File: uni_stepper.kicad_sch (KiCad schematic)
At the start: 2 parts, among them M201 unipolair motor, U201 ULN2003

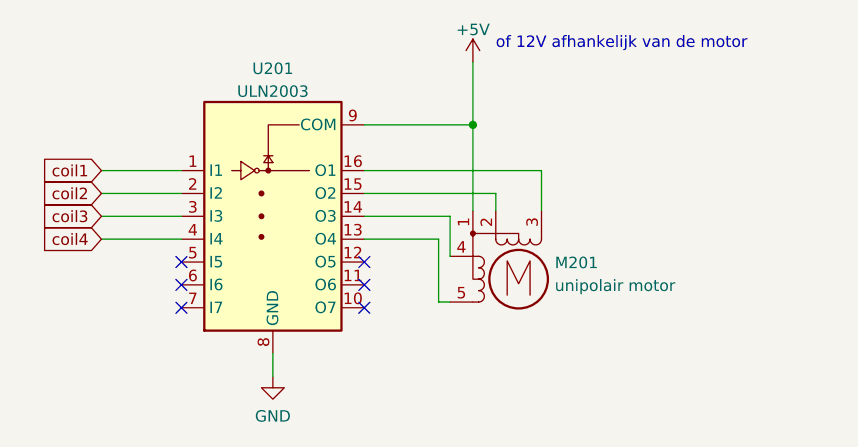
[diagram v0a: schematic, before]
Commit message: added hierarchial labels to some schematics
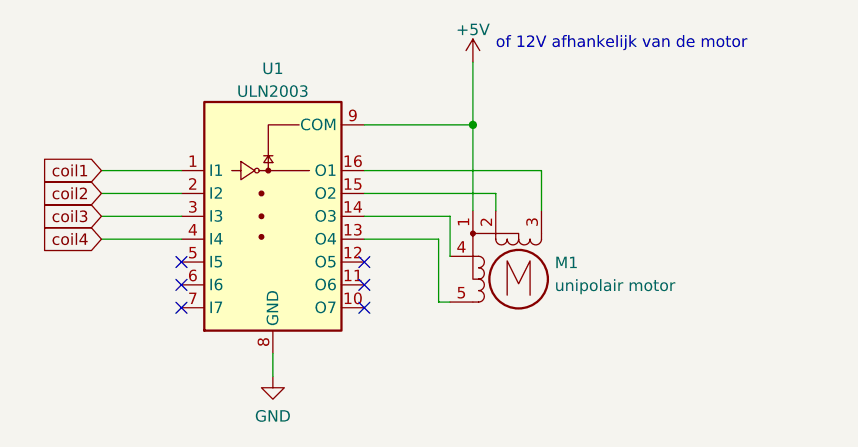
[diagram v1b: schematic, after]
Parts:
- renumbered M201 to M1, U201 to U1
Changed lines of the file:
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@@
-(kicad_sch (version 20211123) (generator eeschema)
+(kicad_sch (version 20230121) (generator eeschema)
   (paper "A4")
   (junction (at 127.635 73.66) (diameter 0) (color 0 0 0 0)
@@
   (no_connect (at 115.57 93.98))
   (wire (pts (xy 86.36 81.28) (xy 95.25 81.28))
-    (stroke (width 0) (type default) (color 0 0 0 0))
+    (stroke (width 0) (type default))
   )
   (wire (pts (xy 127.635 66.675) (xy 127.635 73.66))
-    (stroke (width 0) (type default) (color 0 0 0 0))
+    (stroke (width 0) (type default))
   )
   (wire (pts (xy 86.36 86.36) (xy 95.25 86.36))
-    (stroke (width 0) (type default) (color 0 0 0 0))
+    (stroke (width 0) (type default))
   )
   (wire (pts (xy 115.57 78.74) (xy 135.255 78.74))
-    (stroke (width 0) (type default) (color 0 0 0 0))
+    (stroke (width 0) (type default))
   )
   (wire (pts (xy 86.36 78.74) (xy 95.25 78.74))
-    (stroke (width 0) (type default) (color 0 0 0 0))
+    (stroke (width 0) (type default))
   )
   (wire (pts (xy 123.825 86.36) (xy 115.57 86.36))
-    (stroke (width 0) (type default) (color 0 0 0 0))
+    (stroke (width 0) (type default))
   )
   (wire (pts (xy 125.095 93.345) (xy 123.825 93.345))
-    (stroke (width 0) (type default) (color 0 0 0 0))
+    (stroke (width 0) (type default))
   )
   (wire (pts (xy 135.255 78.74) (xy 135.255 83.185))
-    (stroke (width 0) (type default) (color 0 0 0 0))
+    (stroke (width 0) (type default))
   )
   (wire (pts (xy 125.095 83.82) (xy 115.57 83.82))
-    (stroke (width 0) (type default) (color 0 0 0 0))
+    (stroke (width 0) (type default))
   )
   (wire (pts (xy 127.635 73.66) (xy 127.635 83.185))
-    (stroke (width 0) (type default) (color 0 0 0 0))
+    (stroke (width 0) (type default))
   )
   (wire (pts (xy 130.175 83.185) (xy 130.175 81.28))
-    (stroke (width 0) (type default) (color 0 0 0 0))
+    (stroke (width 0) (type default))
   )
   (wire (pts (xy 86.36 83.82) (xy 95.25 83.82))
-    (stroke (width 0) (type default) (color 0 0 0 0))
+    (stroke (width 0) (type default))
   )
   (wire (pts (xy 115.57 73.66) (xy 127.635 73.66))
-    (stroke (width 0) (type default) (color 0 0 0 0))
+    (stroke (width 0) (type default))
   )
   (wire (pts (xy 105.41 99.06) (xy 105.41 101.6))
-    (stroke (width 0) (type default) (color 0 0 0 0))
+    (stroke (width 0) (type default))
   )
   (wire (pts (xy 123.825 93.345) (xy 123.825 86.36))
-    (stroke (width 0) (type default) (color 0 0 0 0))
+    (stroke (width 0) (type default))
   )
   (wire (pts (xy 130.175 81.28) (xy 115.57 81.28))
-    (stroke (width 0) (type default) (color 0 0 0 0))
+    (stroke (width 0) (type default))
   )
   (wire (pts (xy 125.095 83.82) (xy 125.095 88.265))
-    (stroke (width 0) (type default) (color 0 0 0 0))
+    (stroke (width 0) (type default))
   )
   (text "of 12V afhankelijk van de motor\n" (at 130.175 65.405 0)
@@
   (global_label "coil4" (shape input) (at 86.36 86.36 180) (fields_autoplaced)
     (effects (font (size 1.27 1.27)) (justify right))
-    (property "Intersheet References" "${INTERSHEET_REFS}" (id 0) (at 79.2298 86.2806 0)
+    (property "Intersheetrefs" "${INTERSHEET_REFS}" (at 79.2298 86.2806 0)
       (effects (font (size 1.27 1.27)) (justify right) hide)
     )
@@
   (global_label "coil3" (shape input) (at 86.36 83.82 180) (fields_autoplaced)
     (effects (font (size 1.27 1.27)) (justify right))
-    (property "Intersheet References" "${INTERSHEET_REFS}" (id 0) (at 79.2298 83.7406 0)
+    (property "Intersheetrefs" "${INTERSHEET_REFS}" (at 79.2298 83.7406 0)
       (effects (font (size 1.27 1.27)) (justify right) hide)
     )
@@
   (global_label "coil1" (shape input) (at 86.36 78.74 180) (fields_autoplaced)
     (effects (font (size 1.27 1.27)) (justify right))
-    (property "Intersheet References" "${INTERSHEET_REFS}" (id 0) (at 79.2298 78.6606 0)
+    (property "Intersheetrefs" "${INTERSHEET_REFS}" (at 79.2298 78.6606 0)
       (effects (font (size 1.27 1.27)) (justify right) hide)
     )
@@
   (global_label "coil2" (shape input) (at 86.36 81.28 180) (fields_autoplaced)
     (effects (font (size 1.27 1.27)) (justify right))
-    (property "Intersheet References" "${INTERSHEET_REFS}" (id 0) (at 79.2298 81.2006 0)
+    (property "Intersheetrefs" "${INTERSHEET_REFS}" (at 79.2298 81.2006 0)
       (effects (font (size 1.27 1.27)) (justify right) hide)
     )
   )
   (symbol (lib_id "power:GND") (at 105.41 101.6 0) (unit 1)
-    (in_bom yes) (on_board yes) (fields_autoplaced)
-    (property "Reference" "#PWR0201" (id 0) (at 105.41 107.95 0)
-      (effects (font (size 1.27 1.27)) hide)
-    )
-    (property "Value" "GND" (id 1) (at 105.41 106.0434 0))
-    (property "Footprint" "" (id 2) (at 105.41 101.6 0)
-      (effects (font (size 1.27 1.27)) hide)
-    )
-    (property "Datasheet" "" (id 3) (at 105.41 101.6 0)
-      (effects (font (size 1.27 1.27)) hide)
-    )
-    (pin "1")
+    (in_bom yes) (on_board yes) (dnp no) (fields_autoplaced)
+    (property "Reference" "#PWR02" (at 105.41 107.95 0)
+      (effects (font (size 1.27 1.27)) hide)
+    )
+    (property "Value" "GND" (at 105.41 106.0434 0)
+      (effects (font (size 1.27 1.27)))
+    )
+    (property "Footprint" "" (at 105.41 101.6 0)
+      (effects (font (size 1.27 1.27)) hide)
+    )
+    (property "Datasheet" "" (at 105.41 101.6 0)
+      (effects (font (size 1.27 1.27)) hide)
+    )
+    (pin "1")
+    (instances
+      (project "general_schematics"
+        (path "/e777d9ec-d073-4229-a9e6-2cf85636e407/9476ca91-c6eb-46e7-bd6a-31c98618510b"
+          (reference "#PWR02") (unit 1)
+        )
+      )
+    )
   )
   (symbol (lib_id "Transistor_Array:ULN2003") (at 105.41 83.82 0) (unit 1)
-    (in_bom yes) (on_board yes) (fields_autoplaced)
-    (property "Reference" "U201" (id 0) (at 105.41 67.4202 0))
-    (property "Value" "ULN2003" (id 1) (at 105.41 69.9571 0))
-    (property "Footprint" "" (id 2) (at 106.68 97.79 0)
+    (in_bom yes) (on_board yes) (dnp no) (fields_autoplaced)
+    (property "Reference" "U1" (at 105.41 67.4202 0)
+      (effects (font (size 1.27 1.27)))
+    )
+    (property "Value" "ULN2003" (at 105.41 69.9571 0)
+      (effects (font (size 1.27 1.27)))
+    )
+    (property "Footprint" "" (at 106.68 97.79 0)
       (effects (font (size 1.27 1.27)) (justify left) hide)
     )
-    (property "Datasheet" "http://www.ti.com/lit/ds/symlink/uln2003a.pdf" (id 3) (at 107.95 88.9 0)
+    (property "Datasheet" "http://www.ti.com/lit/ds/symlink/uln2003a.pdf" (at 107.95 88.9 0)
       (effects (font (size 1.27 1.27)) hide)
     )
@@
     (pin "8")
     (pin "9")
+    (instances
+      (project "general_schematics"
+        (path "/e777d9ec-d073-4229-a9e6-2cf85636e407/9476ca91-c6eb-46e7-bd6a-31c98618510b"
+          (reference "U1") (unit 1)
+        )
+      )
+    )
   )
   (symbol (lib_id "Motor:Stepper_Motor_unipolar_5pin") (at 132.715 90.805 0) (unit 1)
-    (in_bom yes) (on_board yes) (fields_autoplaced)
-    (property "Reference" "M201" (id 0) (at 136.7282 88.9924 0)
+    (in_bom yes) (on_board yes) (dnp no) (fields_autoplaced)
+    (property "Reference" "M1" (at 136.7282 88.9924 0)
       (effects (font (size 1.27 1.27)) (justify left))
     )
-    (property "Value" "unipolair motor" (id 1) (at 136.7282 91.5293 0)
+    (property "Value" "unipolair motor" (at 136.7282 91.5293 0)
       (effects (font (size 1.27 1.27)) (justify left))
     )
-    (property "Footprint" "" (id 2) (at 132.969 91.059 0)
-      (effects (font (size 1.27 1.27)) hide)
-    )
-    (property "Datasheet" "http://www.infineon.com/dgdl/Application-Note-TLE8110EE_driving_UniPolarStepperMotor_V1.1.pdf?fileId=db3a30431be39b97011be5d0aa0a00b0" (id 3) (at 132.969 91.059 0)
+    (property "Footprint" "" (at 132.969 91.059 0)
+      (effects (font (size 1.27 1.27)) hide)
+    )
+    (property "Datasheet" "http://www.infineon.com/dgdl/Application-Note-TLE8110EE_driving_UniPolarStepperMotor_V1.1.pdf?fileId=db3a30431be39b97011be5d0aa0a00b0" (at 132.969 91.059 0)
       (effects (font (size 1.27 1.27)) hide)
     )
@@
     (pin "4")
     (pin "5")
+    (instances
+      (project "general_schematics"
+        (path "/e777d9ec-d073-4229-a9e6-2cf85636e407/9476ca91-c6eb-46e7-bd6a-31c98618510b"
+          (reference "M1") (unit 1)
+        )
+      )
+    )
   )
   (symbol (lib_id "power:+5V") (at 127.635 66.675 0) (unit 1)
-    (in_bom yes) (on_board yes) (fields_autoplaced)
-    (property "Reference" "#PWR0202" (id 0) (at 127.635 70.485 0)
-      (effects (font (size 1.27 1.27)) hide)
-    )
-    (property "Value" "+5V" (id 1) (at 127.635 63.0992 0))
-    (property "Footprint" "" (id 2) (at 127.635 66.675 0)
-      (effects (font (size 1.27 1.27)) hide)
-    )
-    (property "Datasheet" "" (id 3) (at 127.635 66.675 0)
-      (effects (font (size 1.27 1.27)) hide)
-    )
-    (pin "1")
+    (in_bom yes) (on_board yes) (dnp no) (fields_autoplaced)
+    (property "Reference" "#PWR01" (at 127.635 70.485 0)
+      (effects (font (size 1.27 1.27)) hide)
+    )
+    (property "Value" "+5V" (at 127.635 63.0992 0)
+      (effects (font (size 1.27 1.27)))
+    )
+    (property "Footprint" "" (at 127.635 66.675 0)
+      (effects (font (size 1.27 1.27)) hide)
+    )
+    (property "Datasheet" "" (at 127.635 66.675 0)
+      (effects (font (size 1.27 1.27)) hide)
+    )
+    (pin "1")
+    (instances
+      (project "general_schematics"
+        (path "/e777d9ec-d073-4229-a9e6-2cf85636e407/9476ca91-c6eb-46e7-bd6a-31c98618510b"
+          (reference "#PWR01") (unit 1)
+        )
+      )
+    )
   )
 )

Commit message: moved some schematic scheets to their own folders and routed a board with it. This allow for re-use of PCB parts.
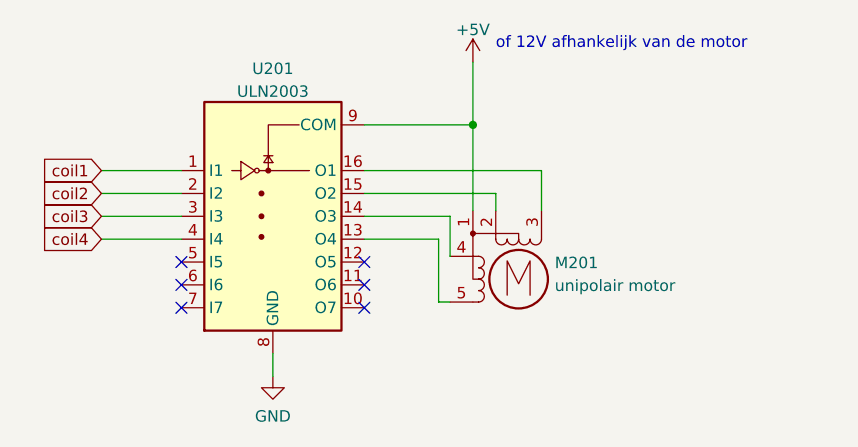
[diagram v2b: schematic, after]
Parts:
- renumbered M1 to M201, U1 to U201
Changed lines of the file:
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@@
   (symbol (lib_id "power:GND") (at 105.41 101.6 0) (unit 1)
     (in_bom yes) (on_board yes) (dnp no) (fields_autoplaced)
-    (property "Reference" "#PWR02" (at 105.41 107.95 0)
+    (property "Reference" "#PWR0101" (at 105.41 107.95 0)
       (effects (font (size 1.27 1.27)) hide)
     )
@@
       (project "general_schematics"
         (path "/e777d9ec-d073-4229-a9e6-2cf85636e407/9476ca91-c6eb-46e7-bd6a-31c98618510b"
-          (reference "#PWR02") (unit 1)
+          (reference "#PWR0101") (unit 1)
         )
       )
@@
   (symbol (lib_id "Transistor_Array:ULN2003") (at 105.41 83.82 0) (unit 1)
     (in_bom yes) (on_board yes) (dnp no) (fields_autoplaced)
-    (property "Reference" "U1" (at 105.41 67.4202 0)
+    (property "Reference" "U201" (at 105.41 67.4202 0)
       (effects (font (size 1.27 1.27)))
     )
@@
       (project "general_schematics"
         (path "/e777d9ec-d073-4229-a9e6-2cf85636e407/9476ca91-c6eb-46e7-bd6a-31c98618510b"
-          (reference "U1") (unit 1)
+          (reference "U201") (unit 1)
         )
       )
@@
   (symbol (lib_id "Motor:Stepper_Motor_unipolar_5pin") (at 132.715 90.805 0) (unit 1)
     (in_bom yes) (on_board yes) (dnp no) (fields_autoplaced)
-    (property "Reference" "M1" (at 136.7282 88.9924 0)
+    (property "Reference" "M201" (at 136.7282 88.9924 0)
       (effects (font (size 1.27 1.27)) (justify left))
     )
@@
       (project "general_schematics"
         (path "/e777d9ec-d073-4229-a9e6-2cf85636e407/9476ca91-c6eb-46e7-bd6a-31c98618510b"
-          (reference "M1") (unit 1)
+          (reference "M201") (unit 1)
         )
       )
@@
   (symbol (lib_id "power:+5V") (at 127.635 66.675 0) (unit 1)
     (in_bom yes) (on_board yes) (dnp no) (fields_autoplaced)
-    (property "Reference" "#PWR01" (at 127.635 70.485 0)
+    (property "Reference" "#PWR0102" (at 127.635 70.485 0)
       (effects (font (size 1.27 1.27)) hide)
     )
@@
       (project "general_schematics"
         (path "/e777d9ec-d073-4229-a9e6-2cf85636e407/9476ca91-c6eb-46e7-bd6a-31c98618510b"
-          (reference "#PWR01") (unit 1)
+          (reference "#PWR0102") (unit 1)
         )
       )
